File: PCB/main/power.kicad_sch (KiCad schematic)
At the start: 21 parts, among them M1 MPMOS, U1 LP2951-3.3_DIP, U2 LM324

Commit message: Add sheet properties
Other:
- title: (none) -> Power Submodule
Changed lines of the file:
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@@
   (paper "A4")
   (title_block
+    (title "Power Submodule")
     (date "2022-03-09")
     (rev "v1.0")
     (company "University of Cape Town")
-    (comment 4 "Authors: Heather WImberley")
+    (comment 1 "Be aware of current loading the volatge input protection circuit")
+    (comment 2 "Schottky diodes can be replaced with a p-channel mosfet configuration")
+    (comment 4 "Authors: Noah Havik")
   )
   (junction (at 210.82 44.45) (diameter 0) (color 0 0 0 0)

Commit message: Add changes
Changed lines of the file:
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@@
+    )
+  )
+  (global_label "GND" (shape input) (at 231.14 148.59 270) (fields_autoplaced)
+    (effects (font (size 1.27 1.27)) (justify right))
+    (property "Intersheet References" "${INTERSHEET_REFS}" (id 0) (at 231.2194 154.8736 90)
+      (effects (font (size 1.27 1.27)) (justify right) hide)
+    )
+  )
+  (global_label "GND" (shape input) (at 176.53 95.25 270) (fields_autoplaced)
+    (effects (font (size 1.27 1.27)) (justify right))
+    (property "Intersheet References" "${INTERSHEET_REFS}" (id 0) (at 176.6094 101.5336 90)
+      (effects (font (size 1.27 1.27)) (justify right) hide)
     )
   )
@@
     (effects (font (size 1.27 1.27)) (justify right))
     (property "Intersheet References" "${INTERSHEET_REFS}" (id 0) (at 23.2288 90.0906 0)
+      (effects (font (size 1.27 1.27)) (justify right) hide)
+    )
+  )
+  (global_label "GND" (shape input) (at 44.45 162.56 270) (fields_autoplaced)
+    (effects (font (size 1.27 1.27)) (justify right))
+    (property "Intersheet References" "${INTERSHEET_REFS}" (id 0) (at 44.5294 168.8436 90)
       (effects (font (size 1.27 1.27)) (justify right) hide)
     )
@@
     (pin "1")
   )
-  (symbol (lib_id "power:GND") (at 44.45 162.56 0) (unit 1)
-    (in_bom yes) (on_board yes) (fields_autoplaced)
-    (property "Reference" "#PWR020" (id 0) (at 44.45 168.91 0)
-      (effects (font (size 1.27 1.27)) hide)
-    )
-    (property "Value" "GND" (id 1) (at 44.45 167.64 0))
-    (property "Footprint" "" (id 2) (at 44.45 162.56 0)
-      (effects (font (size 1.27 1.27)) hide)
-    )
-    (property "Datasheet" "" (id 3) (at 44.45 162.56 0)
-      (effects (font (size 1.27 1.27)) hide)
-    )
-    (pin "1")
-  )
   (symbol (lib_id "Device:R") (at 176.53 67.31 0) (unit 1)
     (in_bom yes) (on_board yes) (fields_autoplaced)
@@
     (pin "1")
     (pin "2")
-  )
-  (symbol (lib_id "power:GND") (at 176.53 95.25 0) (unit 1)
-    (in_bom yes) (on_board yes) (fields_autoplaced)
-    (property "Reference" "#PWR022" (id 0) (at 176.53 101.6 0)
-      (effects (font (size 1.27 1.27)) hide)
-    )
-    (property "Value" "GND" (id 1) (at 176.53 100.33 0))
-    (property "Footprint" "" (id 2) (at 176.53 95.25 0)
-      (effects (font (size 1.27 1.27)) hide)
-    )
-    (property "Datasheet" "" (id 3) (at 176.53 95.25 0)
-      (effects (font (size 1.27 1.27)) hide)
-    )
-    (pin "1")
   )
   (symbol (lib_id "Regulator_Linear:LP2951-3.3_DIP") (at 77.47 129.54 0) (unit 1)
@@
     (pin "2")
   )
-  (symbol (lib_id "power:GND") (at 231.14 148.59 0) (unit 1)
-    (in_bom yes) (on_board yes) (fields_autoplaced)
-    (property "Reference" "#PWR024" (id 0) (at 231.14 154.94 0)
-      (effects (font (size 1.27 1.27)) hide)
-    )
-    (property "Value" "GND" (id 1) (at 231.14 153.67 0))
-    (property "Footprint" "" (id 2) (at 231.14 148.59 0)
-      (effects (font (size 1.27 1.27)) hide)
-    )
-    (property "Datasheet" "" (id 3) (at 231.14 148.59 0)
-      (effects (font (size 1.27 1.27)) hide)
-    )
-    (pin "1")
-  )
   (sheet_instances

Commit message: final changes
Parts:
- BT1: value Battery -> 18650
- D1, D2: value D_Schottky -> BAT54S
- D4: value D_Zener -> ZMM5V1-M
- D6: value 3.3V -> ZMM3V3-M
- M1: value MPMOS -> CJ2301 S1
- U1: value LP2951-3.3_DIP -> LP2951-33DR
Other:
- note added: "Battery Charger"
- note added: "Battery Connection"
- note added: "Battery Polarity Protection"
- note added: "Input Voltage Polarity Protection"
- note added: "Under Voltage Cutout Protection"
- note added: "Voltage Regulator"
- moved on the sheet: BT1, C1, C2, C3, D1, D2, D3, D4, D5, D6, M1, R1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

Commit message: Final Changes
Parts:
- renumbered D6 to D5, D5 to D6
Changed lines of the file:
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@@
+    )
+  )
+  (global_label "GND" (shape input) (at 212.09 55.88 270) (fields_autoplaced)
+    (effects (font (size 1.27 1.27)) (justify right))
+    (property "Intersheet References" "${INTERSHEET_REFS}" (id 0) (at 212.1694 62.1636 90)
+      (effects (font (size 1.27 1.27)) (justify right) hide)
     )
   )
@@
   (symbol (lib_id "Device:D_Zener") (at 215.9 138.43 270) (unit 1)
     (in_bom yes) (on_board yes) (fields_autoplaced)
-    (property "Reference" "D6" (id 0) (at 218.44 137.1599 90)
+    (property "Reference" "D5" (id 0) (at 218.44 137.1599 90)
       (effects (font (size 1.27 1.27)) (justify left))
     )
@@
   (symbol (lib_id "Device:LED") (at 252.73 26.67 0) (unit 1)
     (in_bom yes) (on_board yes) (fields_autoplaced)
-    (property "Reference" "D5" (id 0) (at 251.1425 20.32 0))
+    (property "Reference" "D6" (id 0) (at 251.1425 20.32 0))
     (property "Value" "LED" (id 1) (at 251.1425 22.86 0))
     (property "Footprint" "" (id 2) (at 252.73 26.67 0)
@@
     (pin "2")
   )
-  (symbol (lib_id "power:GND") (at 212.09 55.88 0) (unit 1)
-    (in_bom yes) (on_board yes) (fields_autoplaced)
-    (property "Reference" "#PWR020" (id 0) (at 212.09 62.23 0)
-      (effects (font (size 1.27 1.27)) hide)
-    )
-    (property "Value" "GND" (id 1) (at 212.09 60.96 0))
-    (property "Footprint" "" (id 2) (at 212.09 55.88 0)
-      (effects (font (size 1.27 1.27)) hide)
-    )
-    (property "Datasheet" "" (id 3) (at 212.09 55.88 0)
-      (effects (font (size 1.27 1.27)) hide)
-    )
-    (pin "1")
-  )
   (symbol (lib_id "Device:R") (at 212.09 49.53 0) (unit 1)

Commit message: doink
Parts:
- added JP? (x7): SolderJumper_2_Bridged, symbol Jumper:SolderJumper_2_Bridged
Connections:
- net +5V: now also JP?.1 (A), JP?.1 (A); no longer C1.1, D1.1 (K), D2.2 (A), U1.8 (IN)
- net +5V (INPUT PROTECTED): now also JP?.1 (A); no longer R7.1
- net Battery +: now also JP?.1 (A), JP?.1 (A); no longer D1.2 (A), M1.1 (D), M1.4 (B), R3.1, R5.1, U2.4 (V+)
- net GND: now also JP?.1 (A); no longer BT1.2 (-)
- new net: BT1.2 (-), JP?.2 (B)
- new net: JP?.2 (B), R7.1
- new net: D2.2 (A), JP?.2 (B), JP?.2 (B)
- new net: D1.2 (A), JP?.2 (B)
- new net: C1.1, JP?.2 (B), U1.8 (IN)
- new net: JP?.2 (B), M1.1 (D), M1.4 (B), R3.1, R5.1, U2.4 (V+)
- new net +5V (REVERSE PROTECTED): D1.1 (K), JP?.1 (A)

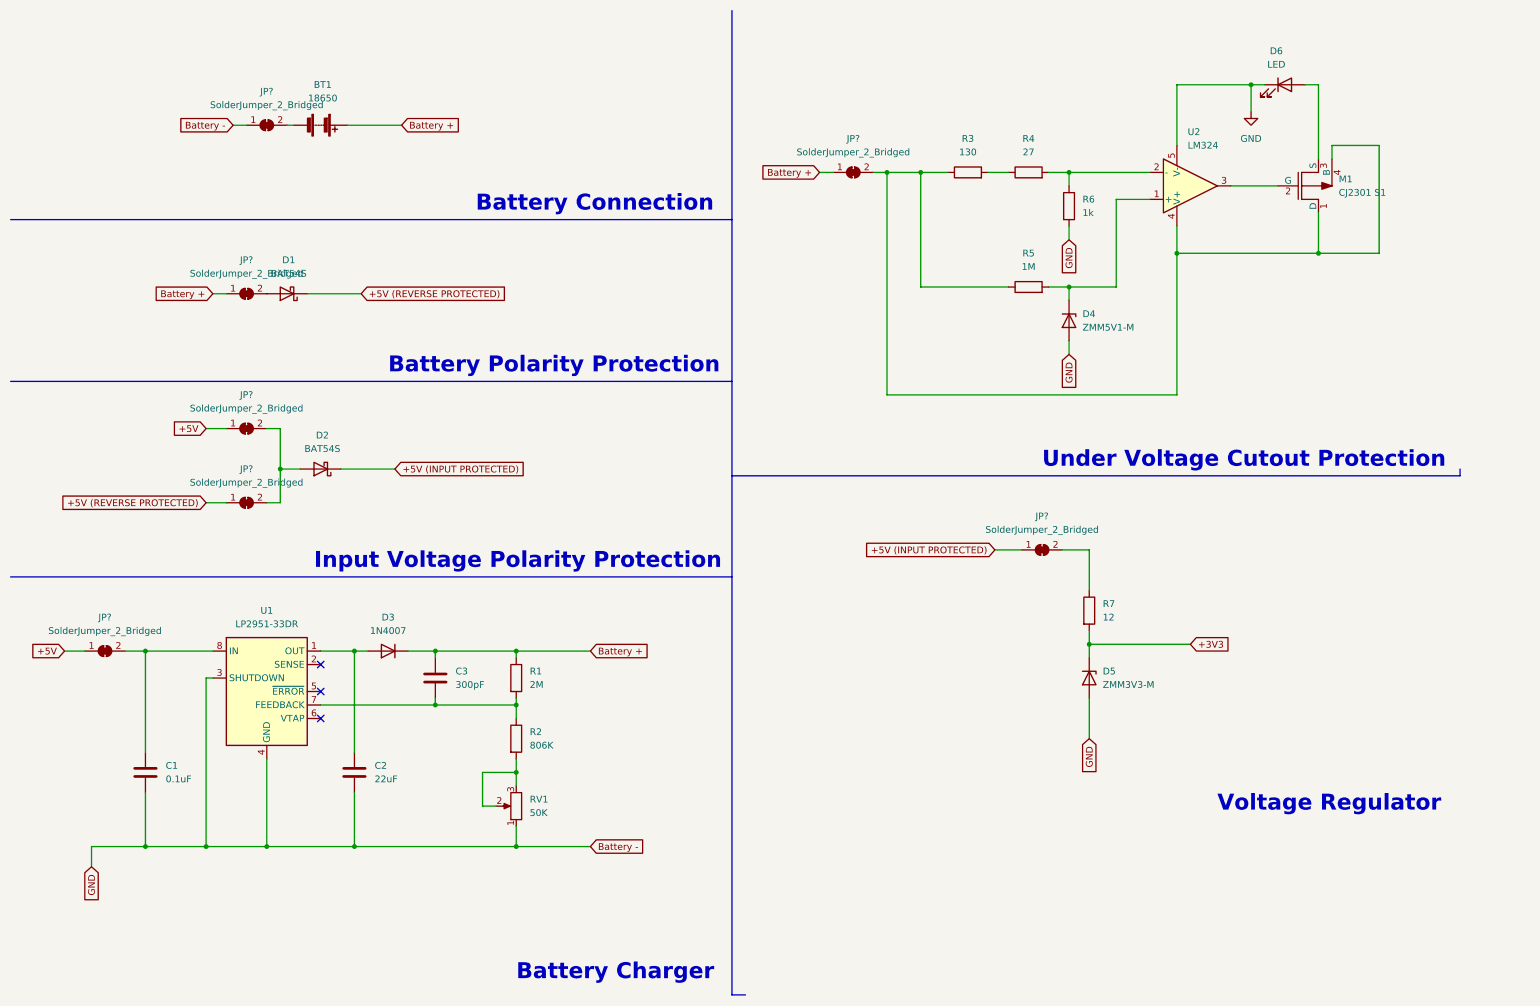
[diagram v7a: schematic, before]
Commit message: Add labels
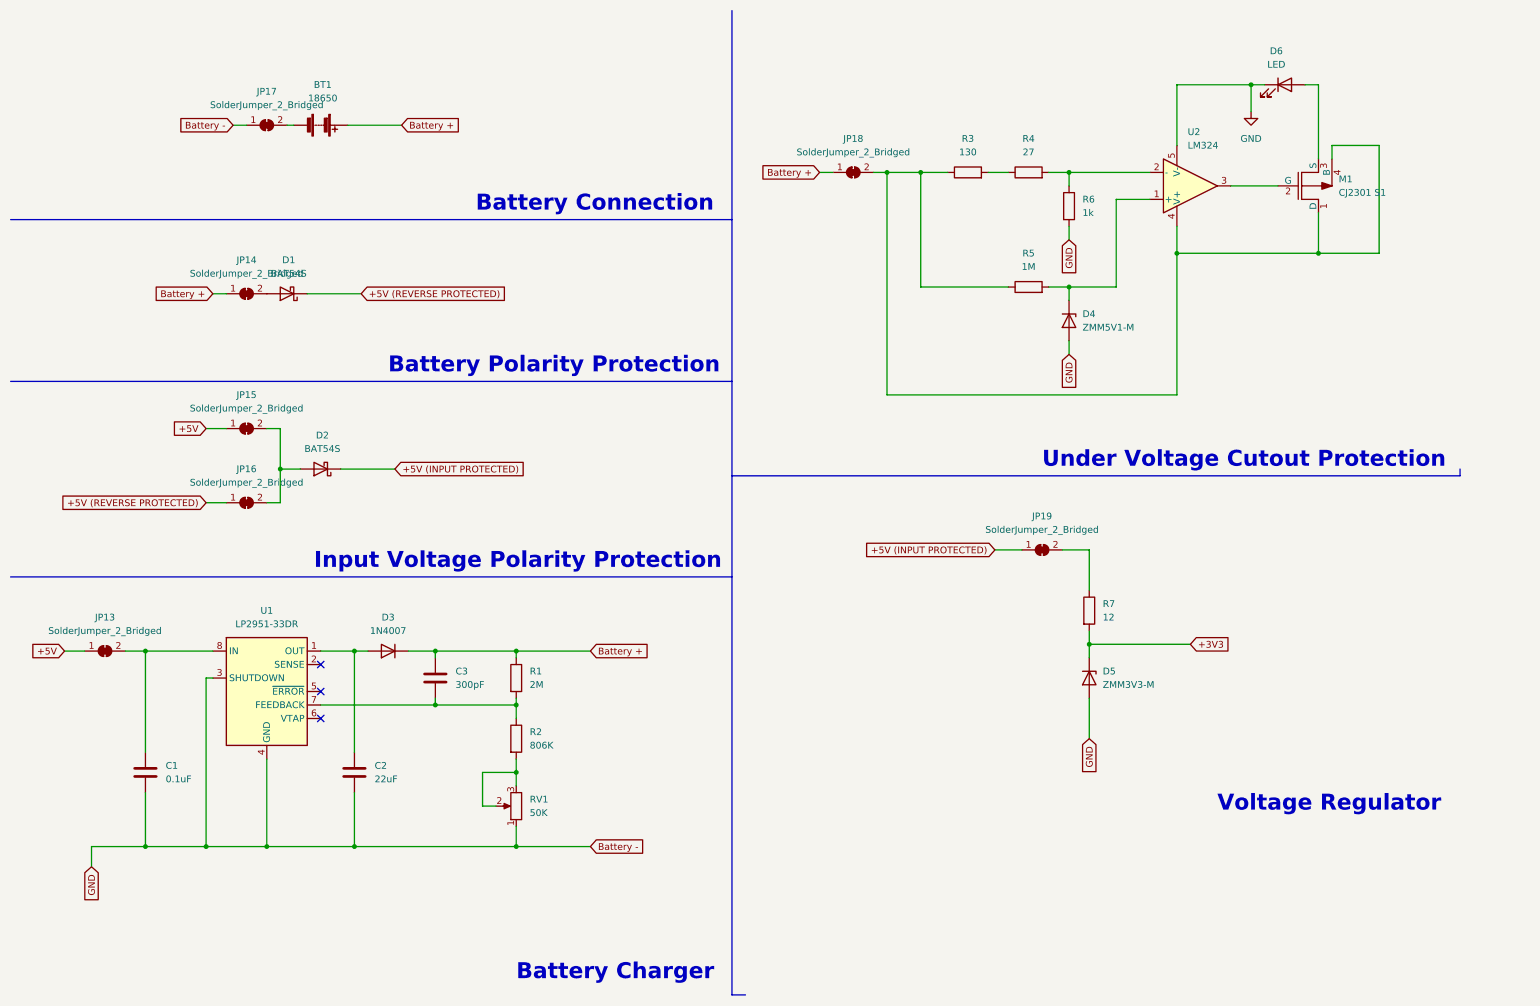
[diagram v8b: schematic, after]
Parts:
- gave numbers to parts that had none: 7
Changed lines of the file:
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@@
   (symbol (lib_id "Jumper:SolderJumper_2_Bridged") (at 60.96 34.29 0) (unit 1)
     (in_bom yes) (on_board yes) (fields_autoplaced)
-    (property "Reference" "JP?" (id 0) (at 60.96 27.94 0))
+    (property "Reference" "JP17" (id 0) (at 60.96 27.94 0))
     (property "Value" "SolderJumper_2_Bridged" (id 1) (at 60.96 30.48 0))
     (property "Footprint" "" (id 2) (at 60.96 34.29 0)
@@
   (symbol (lib_id "Jumper:SolderJumper_2_Bridged") (at 207.01 114.3 0) (unit 1)
     (in_bom yes) (on_board yes) (fields_autoplaced)
-    (property "Reference" "JP?" (id 0) (at 207.01 107.95 0))
+    (property "Reference" "JP19" (id 0) (at 207.01 107.95 0))
     (property "Value" "SolderJumper_2_Bridged" (id 1) (at 207.01 110.49 0))
     (property "Footprint" "" (id 2) (at 207.01 114.3 0)
@@
   (symbol (lib_id "Jumper:SolderJumper_2_Bridged") (at 57.15 66.04 0) (unit 1)
     (in_bom yes) (on_board yes) (fields_autoplaced)
-    (property "Reference" "JP?" (id 0) (at 57.15 59.69 0))
+    (property "Reference" "JP14" (id 0) (at 57.15 59.69 0))
     (property "Value" "SolderJumper_2_Bridged" (id 1) (at 57.15 62.23 0))
     (property "Footprint" "" (id 2) (at 57.15 66.04 0)
@@
   (symbol (lib_id "Jumper:SolderJumper_2_Bridged") (at 57.15 105.41 0) (unit 1)
     (in_bom yes) (on_board yes) (fields_autoplaced)
-    (property "Reference" "JP?" (id 0) (at 57.15 99.06 0))
+    (property "Reference" "JP16" (id 0) (at 57.15 99.06 0))
     (property "Value" "SolderJumper_2_Bridged" (id 1) (at 57.15 101.6 0))
     (property "Footprint" "" (id 2) (at 57.15 105.41 0)
@@
   (symbol (lib_id "Jumper:SolderJumper_2_Bridged") (at 30.48 133.35 0) (unit 1)
     (in_bom yes) (on_board yes) (fields_autoplaced)
-    (property "Reference" "JP?" (id 0) (at 30.48 127 0))
+    (property "Reference" "JP13" (id 0) (at 30.48 127 0))
     (property "Value" "SolderJumper_2_Bridged" (id 1) (at 30.48 129.54 0))
     (property "Footprint" "" (id 2) (at 30.48 133.35 0)
@@
   (symbol (lib_id "Jumper:SolderJumper_2_Bridged") (at 171.45 43.18 0) (unit 1)
     (in_bom yes) (on_board yes) (fields_autoplaced)
-    (property "Reference" "JP?" (id 0) (at 171.45 36.83 0))
+    (property "Reference" "JP18" (id 0) (at 171.45 36.83 0))
     (property "Value" "SolderJumper_2_Bridged" (id 1) (at 171.45 39.37 0))
     (property "Footprint" "" (id 2) (at 171.45 43.18 0)
@@
   (symbol (lib_id "Jumper:SolderJumper_2_Bridged") (at 57.15 91.44 0) (unit 1)
     (in_bom yes) (on_board yes) (fields_autoplaced)
-    (property "Reference" "JP?" (id 0) (at 57.15 85.09 0))
+    (property "Reference" "JP15" (id 0) (at 57.15 85.09 0))
     (property "Value" "SolderJumper_2_Bridged" (id 1) (at 57.15 87.63 0))
     (property "Footprint" "" (id 2) (at 57.15 91.44 0)
